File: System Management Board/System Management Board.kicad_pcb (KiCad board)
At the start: 4 copper layers, 150 x 110 mm, 138 parts, among them IC1 SI2318CDS-T1-GE3, IC2 SI2318CDS-T1-GE3, IC3 SI2318CDS-T1-GE3, IC4 SI2318CDS-T1-GE3, IC5 SI2318CDS-T1-GE3, IC6 SI2318CDS-T1-GE3, J1 Conn_01x04_Male, J10 Conn_01x02_Male, J11 Conn_02x20_Odd_Even, J12 Conn_02x05_Top_Bottom, J13 Conn_01x04_Female, J2 Conn_01x04_Male, J3 Conn_01x02_Male, J4 PJ-063BH, J5 Conn_01x02_Male, J6 Conn_02x06_Counter_Clockwise, J7 Conn_02x20_Odd_Even, J8 Conn_01x02_Male, J9 Conn_01x02_Male, K1 J115F11CH5VDCS61.5U, K2 J114FL1CS165VDC.41, K3 J114FL1CS165VDC.41, SW1 SW_Push, SW2 SW_Push, U1 SC0915, U4 R1560S501B-E2-FE, U5 74HC4051, U6 MCP9700T-ETT, U7 MCP9700T-ETT

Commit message: Pushing most recent, no significant changes
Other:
- board text added: "System Management Board V0.3 7-30-2024 -- M. Funderburk, C. Nichols Precision Sustainable Agriculture"
- board text removed: "System Management Board V0.3 7-3-2024 -- M. Funderburk, C. Nichols Precision Sustainable Agriculture"
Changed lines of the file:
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@@
 		)
 	)
-	(gr_text "System Management Board V0.3\n7-3-2024 -- M. Funderburk, C. Nichols\nPrecision Sustainable Agriculture"
+	(gr_text "System Management Board V0.3\n7-30-2024 -- M. Funderburk, C. Nichols\nPrecision Sustainable Agriculture"
 		(at 209.683 75.572 0)
 		(layer "B.SilkS")

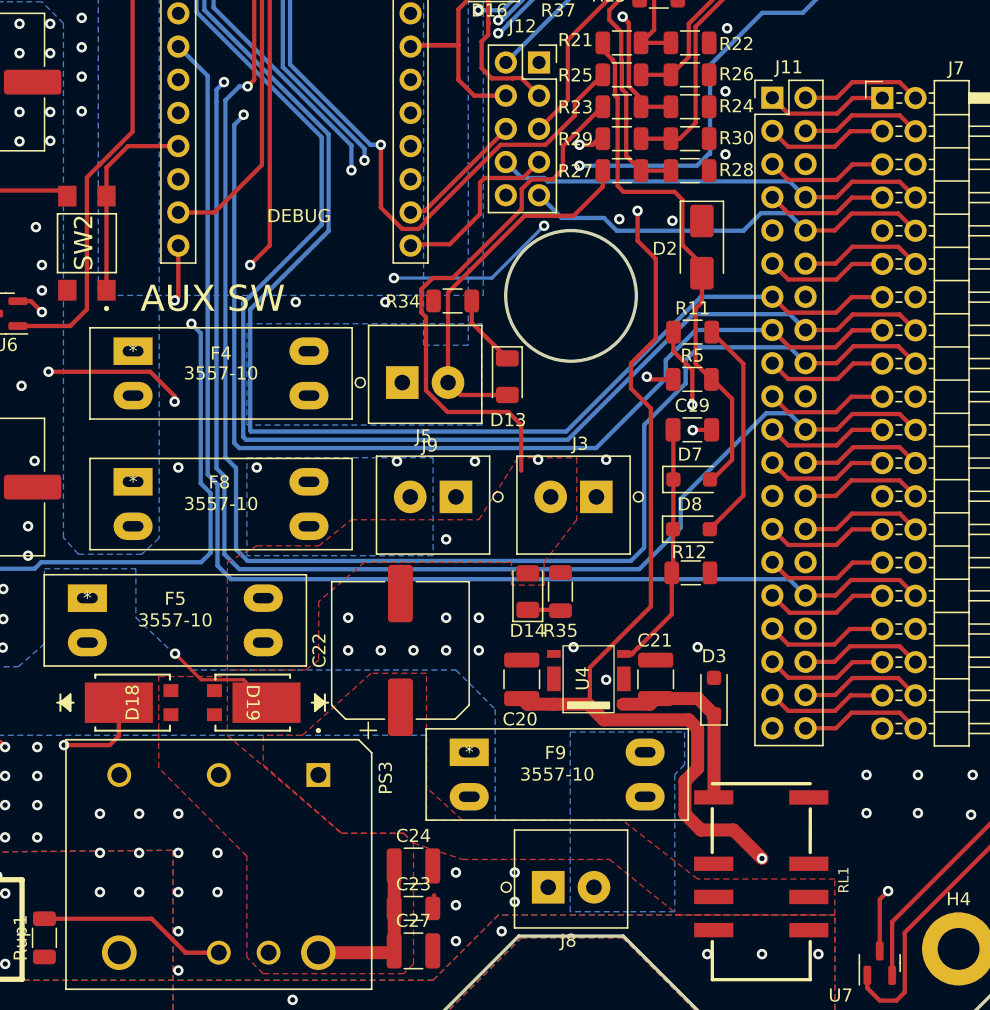
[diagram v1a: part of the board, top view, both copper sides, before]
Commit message: testing points added
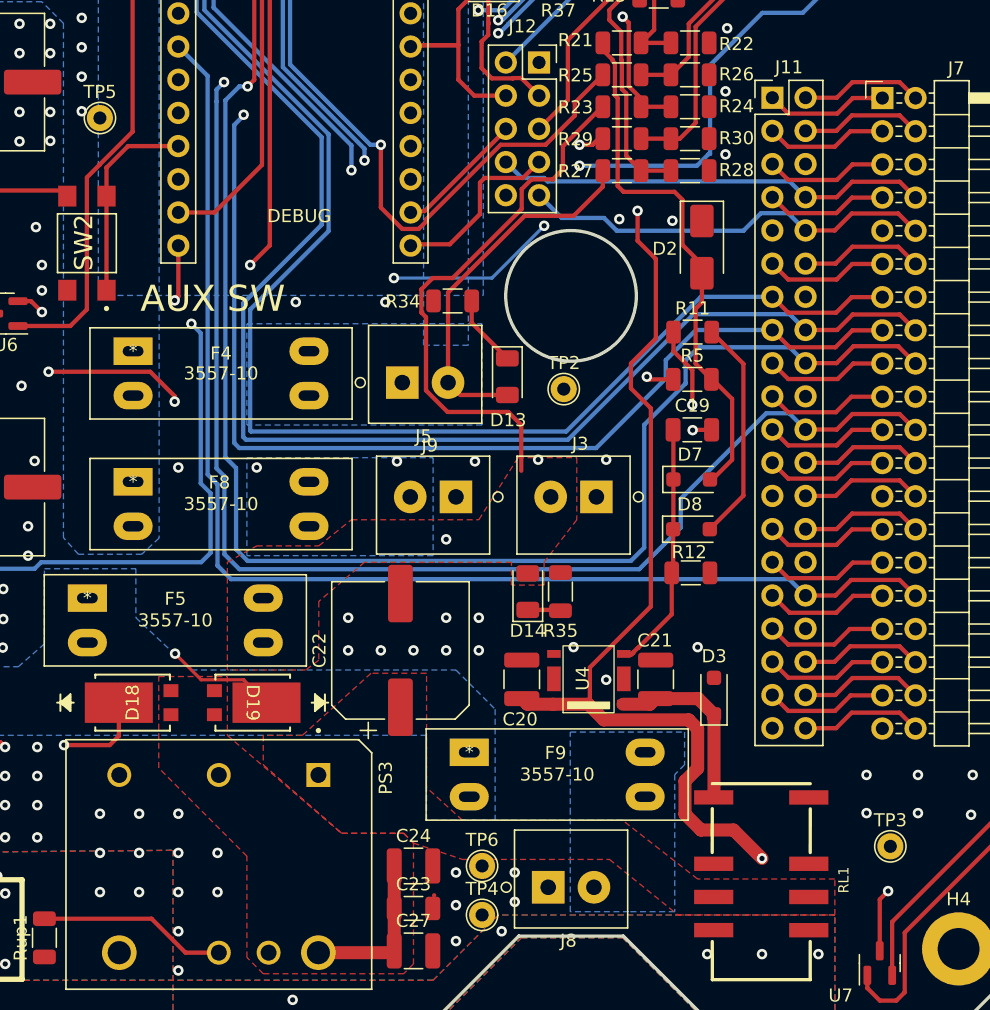
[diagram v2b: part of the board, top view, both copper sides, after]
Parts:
- added TP2: KeySwitch IN, TestPoint:TestPoint_THTPad_D2.0mm_Drill1.0mm, F.Cu at (186.5, 107.5)
- added TP3: TestPoint, TestPoint:TestPoint_THTPad_D2.0mm_Drill1.0mm, F.Cu at (211.5, 142.5)
- added TP4: TestPoint, TestPoint:TestPoint_THTPad_D2.0mm_Drill1.0mm, F.Cu at (180.2, 147.8)
- added TP5: TestPoint, TestPoint:TestPoint_THTPad_D2.0mm_Drill1.0mm, F.Cu at (151.0, 86.8)
- added TP6: TestPoint, TestPoint:TestPoint_THTPad_D2.0mm_Drill1.0mm, F.Cu at (180.2, 144.0)
- R21, R25, R27, R29: value 100k -> 220k

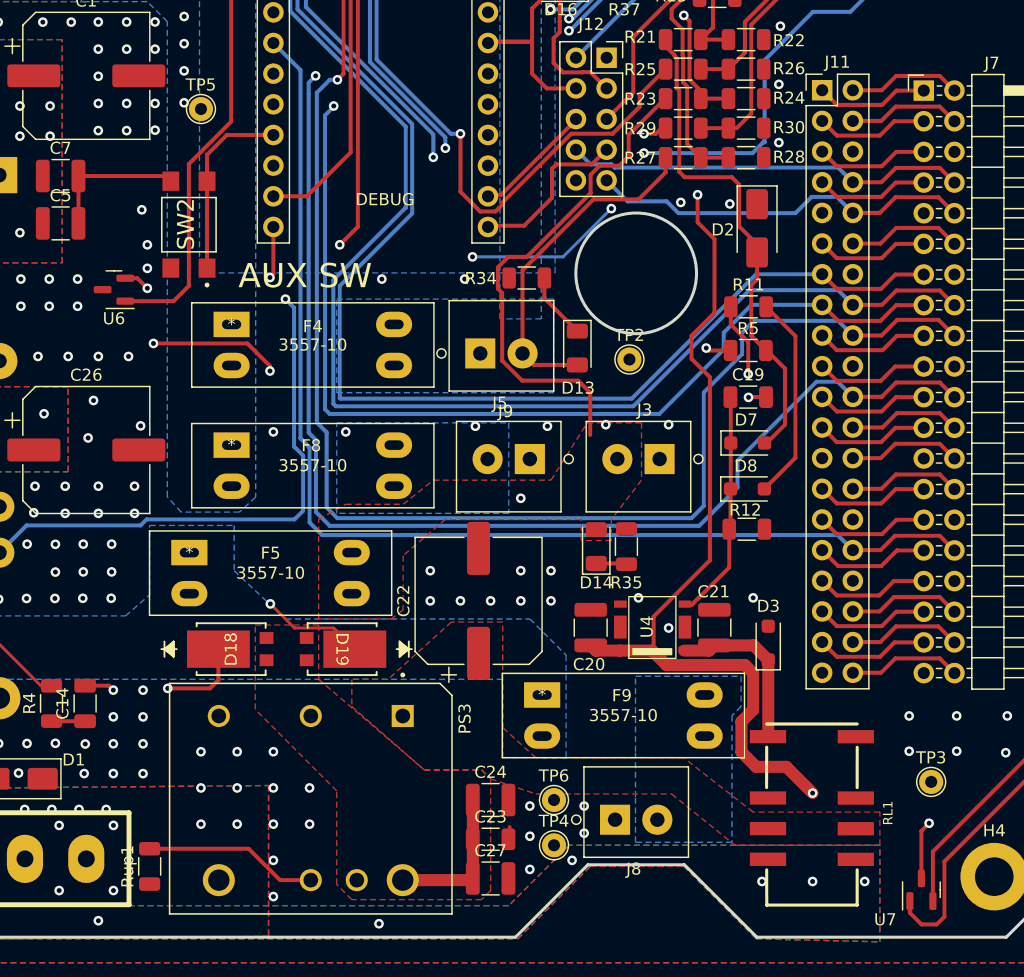
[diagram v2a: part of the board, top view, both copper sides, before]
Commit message: pushing all test pt mods
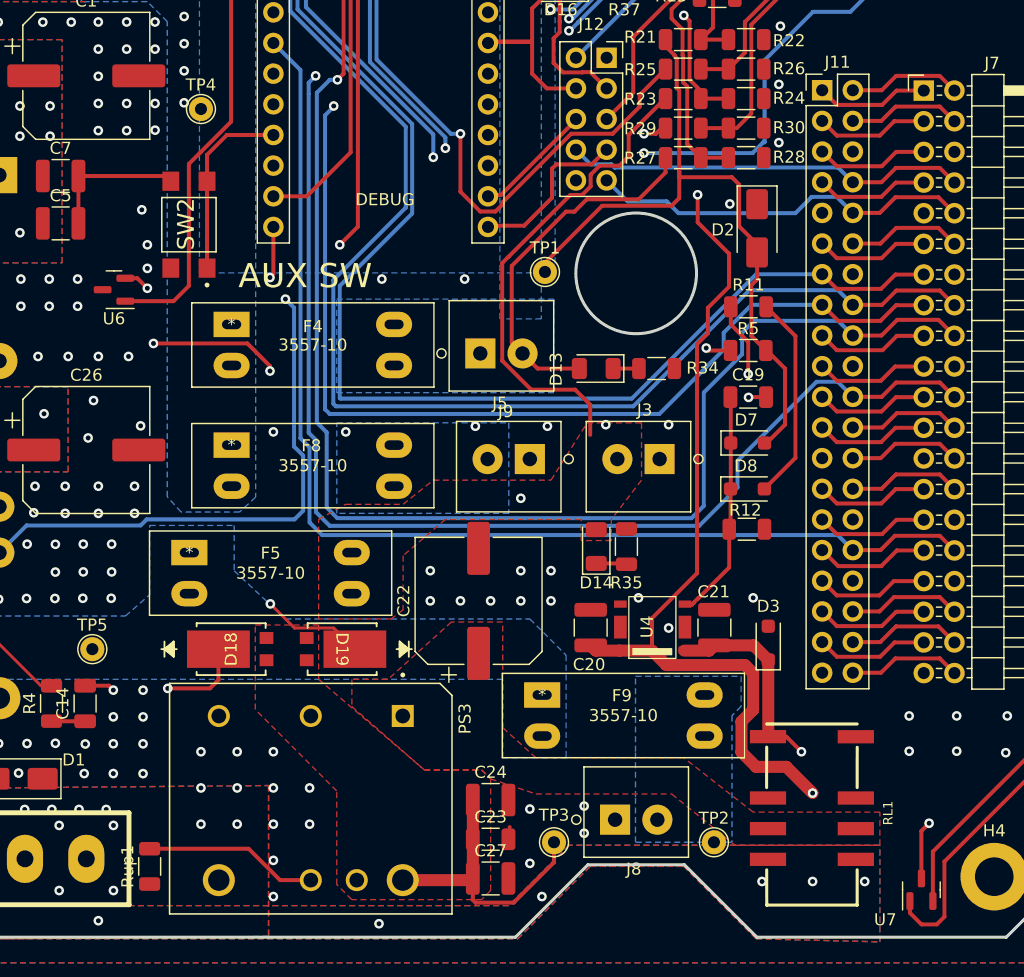
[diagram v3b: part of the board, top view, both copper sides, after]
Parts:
- moved TP5 40.2 mm to (142.0, 131.5)
- moved TP2 18.7 mm to (193.5, 147.5)
- moved R34 13.1 mm to (188.8, 108.2), turned to 0 degrees
- moved TP1 10.1 mm to (179.5, 100.2)
- moved D13 2.31 mm to (183.8, 108.2), turned to 180 degrees
- moved TP3 0.25 mm to (180.2, 147.5), turned to 180 degrees
- renumbered TP2 to TP1, TP3 to TP2, TP4 to TP3, TP5 to TP4, TP6 to TP5
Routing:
- net /KeySwitch IN: track 40.8 -> 57.3 mm
- net /5V BOOTSTRAP: track 14.4 -> 30.0 mm, vias 0 -> 1
- net /5V Intermediate: track 12.4 -> 24.1 mm
- net Net-(D13-K): track 5.53 -> 2.14 mm
- net /COMP PWR OUT PROT: track 29.1 -> 30.8 mm
- net /SWITCH PWR OUT PROT: track 41.3 -> 40.1 mm
- net /Aux_SW: track 101.3 -> 101.0 mm, vias 3 -> 1
- net GND: vias 350 -> 348
